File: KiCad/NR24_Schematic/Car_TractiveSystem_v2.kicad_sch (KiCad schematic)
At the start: 14 parts, among them J1 M_con, J2 F_con, K2 Key Switch Relay, M1 Zero_7R_Motor, SW3 100V E-stop (Right), SW4 100V E-stop (Left), SW7 TI power switch, U1 Sevcon_Gen4_Size6, U2 Throttle, U7 Brake (AiM Pressure Sensor)

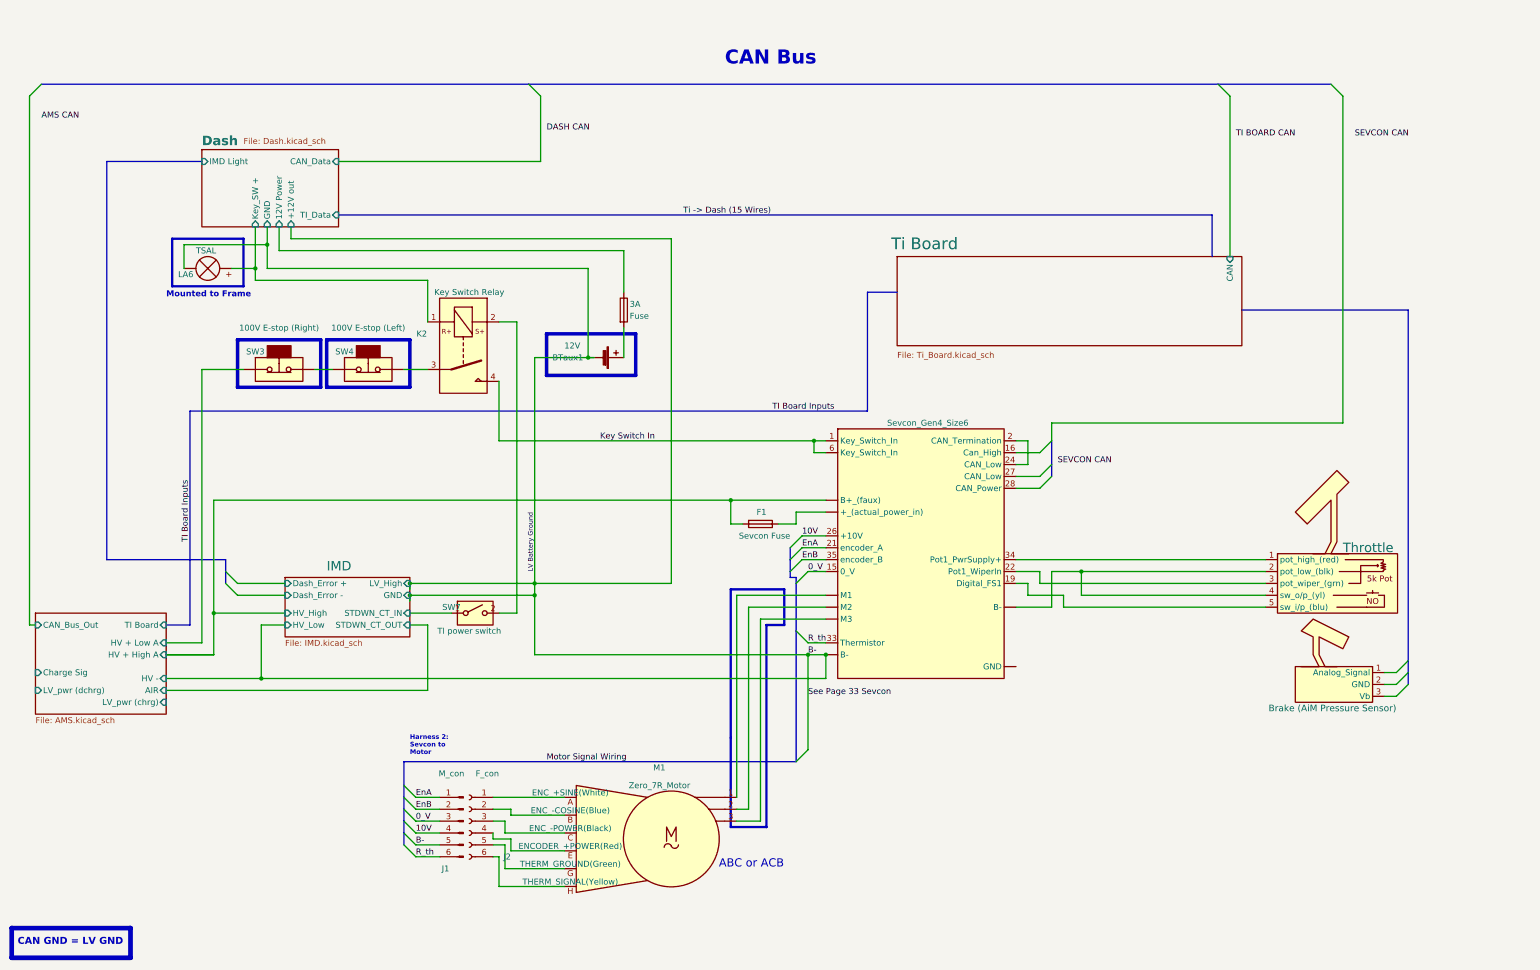
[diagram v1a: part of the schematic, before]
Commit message: AMS with relay
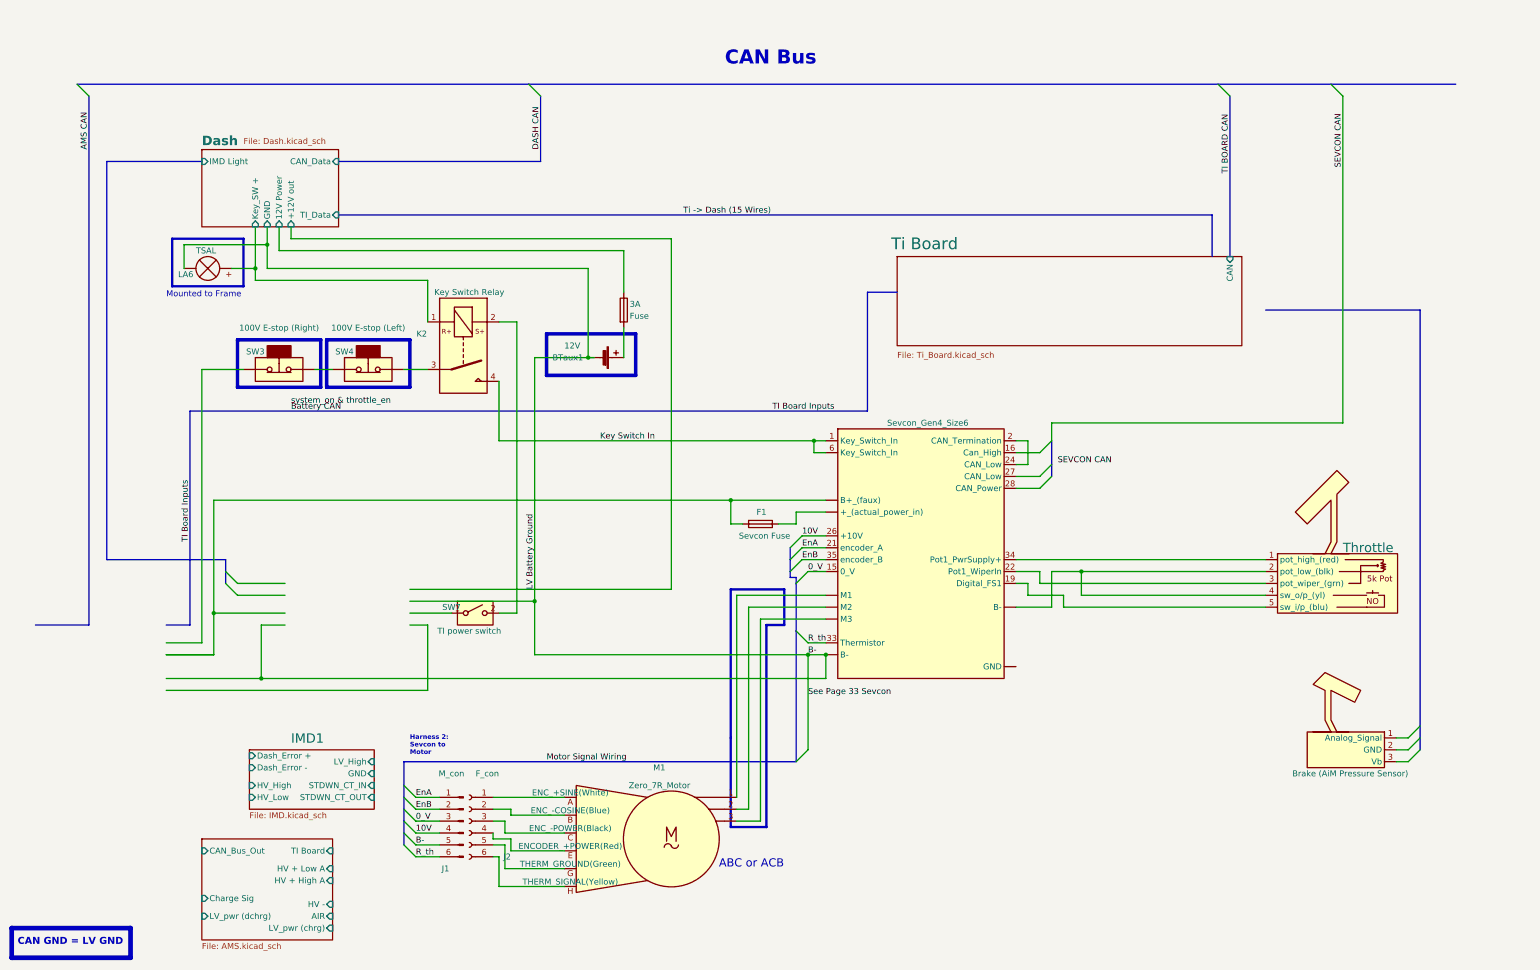
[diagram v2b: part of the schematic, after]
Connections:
- net AMS & Battery/HV + High A: no longer names the net of F1.2, U1. (M3)
- net AMS & Battery/HV + Low A: no longer names the net of SW3.1 (A)
- net IMD/STDWN_CT_IN: no longer names the net of SW7.1 (A)
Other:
- removed sheet AMS & Battery
- removed sheet IMD
- added sheet AMS & Battery1 (AMS.kicad_sch)
- added sheet IMD1 (IMD.kicad_sch)

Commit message: new sheet
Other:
- added sheet Battery_Low_Side (Batter_Low_Side.kicad_sch)
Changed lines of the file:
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@@
+    )
+  )
+  (sheet (at 29.21 238.76) (size 22.86 21.59) (fields_autoplaced)
+    (stroke (width 0.1524) (type solid))
+    (fill (color 0 0 0 0.0000))
+    (property "Sheetname" "Battery_Low_Side" (at 29.21 238.0484 0)
+      (effects (font (size 1.27 1.27)) (justify left bottom))
+    )
+    (property "Sheetfile" "Batter_Low_Side.kicad_sch" (at 29.21 260.9346 0)
+      (effects (font (size 1.27 1.27)) (justify left top))
+    )
+    (instances
+      (project "Car_TractiveSystem_v2"
+        (path "/588b5c14-1813-4e1d-9dbe-940839ecebe3" (page "6"))
+      )
     )
   )

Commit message: root
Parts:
- added SW8: GLVMS, symbol CamachosSymbols:SW_SPST
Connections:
- net at K2.3: no longer SW4.2 (B)
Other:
- moved on the sheet: SW3, SW4

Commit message: root
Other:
- note added: "change"
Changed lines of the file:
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@@
     (effects (font (size 1.27 1.27)) (justify left top))
+  )
+  (text "change" (at 73.66 73.66 0)
+    (effects (font (size 1.27 1.27)) (justify left bottom))
   )
   (text "Mounted to Frame" (at 45.72 146.05 0)

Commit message: ...
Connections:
- net LOW AMPs HIGH VOLT: now reaches K2.3
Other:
- removed sheet IMD1
- sheet AMS & Battery1 ports: added Dash_Error +, Dash_Error -, GND, LV_High, STDWN_CT_OUT2; removed AIR, LV_pwr (chrg), LV_pwr (dchrg), TI Board
- sheet Battery_Low_Side ports: added CAN_Bus_Out, Charge Sig, Dash_Error +, Dash_Error -, GND, HV +, HV -, LV_pwr, STDWN_CT_OUT; removed none
- note removed: "change"

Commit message: update
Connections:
- net B-: no longer BTaux1.2 (-), LA6.1 (-)
- new net LV Battery Ground: BTaux1.2 (-), LA6.1 (-)
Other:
- sheet Battery_Low_Side renamed Battery_Low
- sheet Battery_Low: file Batter_Low_Side.kicad_sch -> Battery_Low.kicad_sch
- sheet Battery_Low ports: added LV_High; removed LV_pwr
- moved on the sheet: J1, J2, M1
